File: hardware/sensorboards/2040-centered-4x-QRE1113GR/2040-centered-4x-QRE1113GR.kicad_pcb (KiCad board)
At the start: 2 copper layers, 49 x 46.5 mm, 15 parts, among them J1 Conn_01x10_Male, U1 QRE1113GR, U2 QRE1113GR, U3 QRE1113GR, U4 QRE1113GR

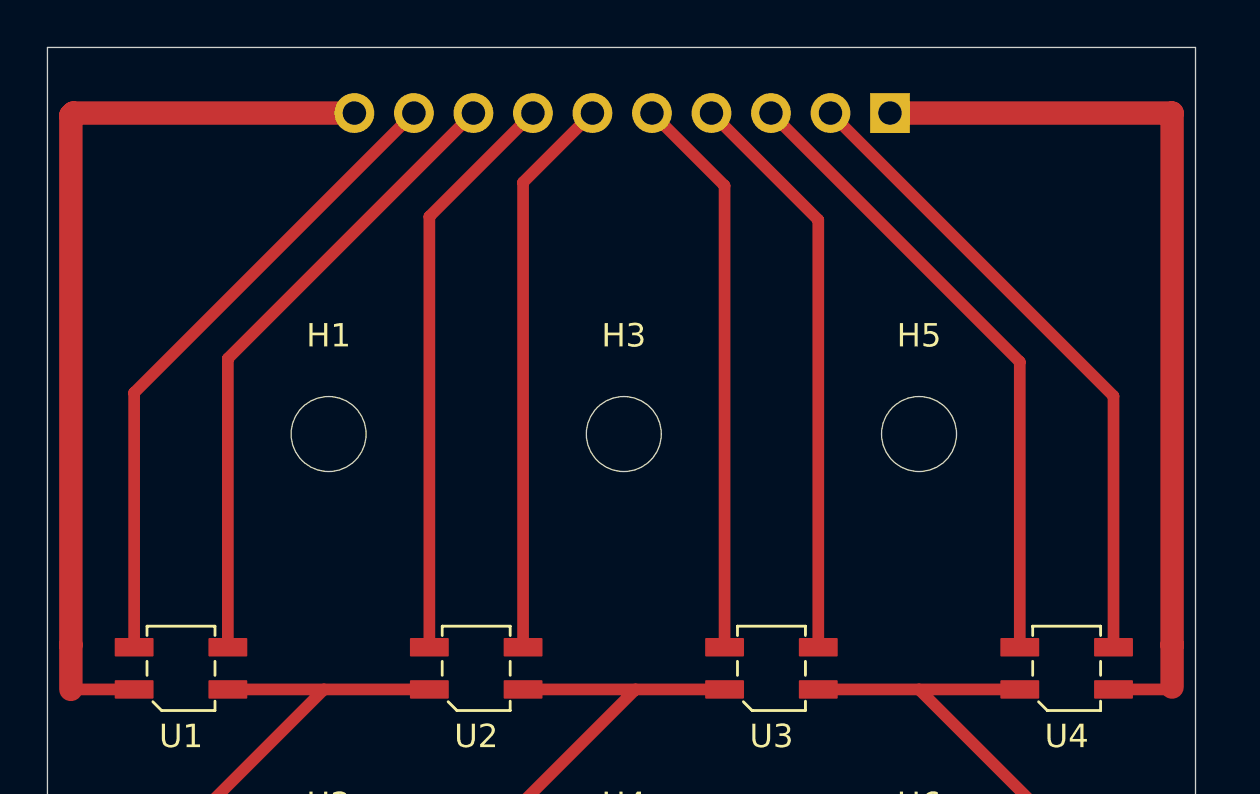
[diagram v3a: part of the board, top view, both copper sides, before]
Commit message: further suggestions from https://pianoclack.com/forum/d/542-update-on-piano-conversion/14
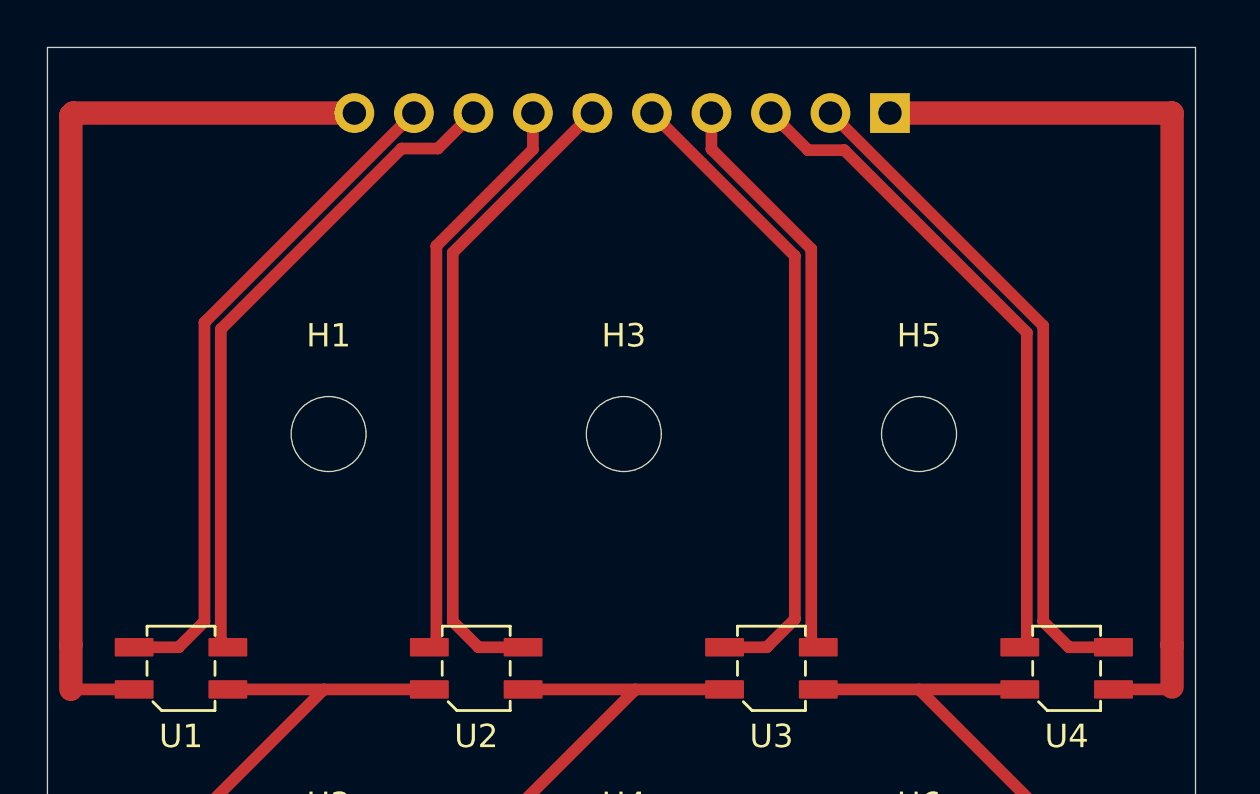
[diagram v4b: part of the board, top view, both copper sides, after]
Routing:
- net Net-(U2-Pad3): track 24.0 -> 27.6 mm
- net /E3: track 24.3 -> 27.6 mm
- net /E4: track 27.2 -> 28.4 mm
- net /C1: track 27.1 -> 28.3 mm
- net /E1: track 27.7 -> 28.9 mm
- net /C4: track 28.2 -> 28.9 mm
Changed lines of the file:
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@@
   (segment (start 159.5 92.9) (end 161.9 92.9) (width 0.5) (layer "F.Cu") (net 1))
   (segment (start 161.9 92.9) (end 162 92.8) (width 0.5) (layer "F.Cu") (net 1))
-  (segment (start 155.5 78.92) (end 155.5 91.1) (width 0.5) (layer "F.Cu") (net 2))
-  (segment (start 144.88 68.3) (end 155.5 78.92) (width 0.5) (layer "F.Cu") (net 2))
-  (segment (start 159.5 80.38) (end 147.42 68.3) (width 0.5) (layer "F.Cu") (net 3))
-  (segment (start 159.5 91.1) (end 159.5 80.38) (width 0.5) (layer "F.Cu") (net 3))
-  (segment (start 159.5 91.1) (end 159.1 91.1) (width 0.5) (layer "F.Cu") (net 3))
-  (segment (start 142.9 71.4) (end 142.9 91.1) (width 0.5) (layer "F.Cu") (net 4))
-  (segment (start 139.8 68.3) (end 142.9 71.4) (width 0.5) (layer "F.Cu") (net 4))
-  (segment (start 140 68.535) (end 139.84 68.375) (width 0.5) (layer "F.Cu") (net 4))
-  (segment (start 146.9 72.86) (end 146.9 91.1) (width 0.5) (layer "F.Cu") (net 5))
-  (segment (start 142.34 68.3) (end 146.9 72.86) (width 0.5) (layer "F.Cu") (net 5))
-  (segment (start 130.3 72.72) (end 130.3 91.1) (width 0.5) (layer "F.Cu") (net 6))
-  (segment (start 134.72 68.3) (end 130.3 72.72) (width 0.5) (layer "F.Cu") (net 6))
-  (segment (start 117.7 80.24) (end 129.64 68.3) (width 0.5) (layer "F.Cu") (net 7))
-  (segment (start 117.7 91.1) (end 117.7 80.24) (width 0.5) (layer "F.Cu") (net 7))
-  (segment (start 121.7 78.78) (end 121.7 91.1) (width 0.5) (layer "F.Cu") (net 8))
-  (segment (start 132.18 68.3) (end 121.7 78.78) (width 0.5) (layer "F.Cu") (net 8))
+  (segment (start 155.8 90.8) (end 155.8 77.66927) (width 0.5) (layer "F.Cu") (net 2))
+  (segment (start 146.464635 69.884635) (end 144.88 68.3) (width 0.5) (layer "F.Cu") (net 2))
+  (segment (start 155.8 77.66927) (end 148.015365 69.884635) (width 0.5) (layer "F.Cu") (net 2))
+  (segment (start 148.015365 69.884635) (end 146.464635 69.884635) (width 0.5) (layer "F.Cu") (net 2))
+  (segment (start 155.5 91.1) (end 155.8 90.8) (width 0.5) (layer "F.Cu") (net 2))
+  (segment (start 157.59952 91.1) (end 159.5 91.1) (width 0.5) (layer "F.Cu") (net 3))
+  (segment (start 147.42 68.3) (end 156.49952 77.37952) (width 0.5) (layer "F.Cu") (net 3))
+  (segment (start 156.49952 77.37952) (end 156.49952 90) (width 0.5) (layer "F.Cu") (net 3))
+  (segment (start 156.49952 90) (end 157.59952 91.1) (width 0.5) (layer "F.Cu") (net 3))
+  (segment (start 145.90048 89.89952) (end 144.7 91.1) (width 0.5) (layer "F.Cu") (net 4))
+  (segment (start 145.90048 74.40048) (end 139.8 68.3) (width 0.5) (layer "F.Cu") (net 4))
+  (segment (start 144.7 91.1) (end 142.9 91.1) (width 0.5) (layer "F.Cu") (net 4))
+  (segment (start 145.90048 74.40048) (end 145.90048 89.89952) (width 0.5) (layer "F.Cu") (net 4))
+  (segment (start 142.34 69.84) (end 146.6 74.1) (width 0.5) (layer "F.Cu") (net 5))
+  (segment (start 142.34 68.3) (end 142.34 69.84) (width 0.5) (layer "F.Cu") (net 5))
+  (segment (start 146.6 90.8) (end 146.9 91.1) (width 0.5) (layer "F.Cu") (net 5))
+  (segment (start 146.6 74.1) (end 146.6 90.8) (width 0.5) (layer "F.Cu") (net 5))
+  (segment (start 130.6 90.8) (end 130.6 73.97073) (width 0.5) (layer "F.Cu") (net 6))
+  (segment (start 134.72 69.85073) (end 134.72 68.3) (width 0.5) (layer "F.Cu") (net 6))
+  (segment (start 130.6 73.97073) (end 134.72 69.85073) (width 0.5) (layer "F.Cu") (net 6))
+  (segment (start 130.3 91.1) (end 130.6 90.8) (width 0.5) (layer "F.Cu") (net 6))
+  (segment (start 129.64 68.3) (end 120.700481 77.239519) (width 0.5) (layer "F.Cu") (net 7))
+  (segment (start 120.700481 89.999519) (end 119.6 91.1) (width 0.5) (layer "F.Cu") (net 7))
+  (segment (start 120.700481 77.239519) (end 120.700481 89.999519) (width 0.5) (layer "F.Cu") (net 7))
+  (segment (start 119.6 91.1) (end 117.7 91.1) (width 0.5) (layer "F.Cu") (net 7))
+  (segment (start 129.114635 69.814635) (end 121.4 77.52927) (width 0.5) (layer "F.Cu") (net 8))
+  (segment (start 121.4 90.8) (end 121.7 91.1) (width 0.5) (layer "F.Cu") (net 8))
+  (segment (start 121.4 77.52927) (end 121.4 90.8) (width 0.5) (layer "F.Cu") (net 8))
+  (segment (start 130.665365 69.814635) (end 129.114635 69.814635) (width 0.5) (layer "F.Cu") (net 8))
+  (segment (start 132.18 68.3) (end 130.665365 69.814635) (width 0.5) (layer "F.Cu") (net 8))
   (segment (start 115 92.9) (end 117.7 92.9) (width 0.5) (layer "F.Cu") (net 9))
   (segment (start 115.1 68.3) (end 127.1 68.3) (width 1) (layer "F.Cu") (net 9))
@@
   (segment (start 146.9 92.9) (end 155.5 92.9) (width 0.5) (layer "F.Cu") (net 12))
   (segment (start 158 99.7) (end 151.2 92.9) (width 0.5) (layer "F.Cu") (net 12))
-  (segment (start 137.26 68.3) (end 134.3 71.26) (width 0.5) (layer "F.Cu") (net 13))
-  (segment (start 134.3 71.26) (end 134.3 91.1) (width 0.5) (layer "F.Cu") (net 13))
+  (segment (start 131.29952 74.26048) (end 131.29952 90) (width 0.5) (layer "F.Cu") (net 13))
+  (segment (start 132.39952 91.1) (end 134.3 91.1) (width 0.5) (layer "F.Cu") (net 13))
+  (segment (start 137.26 68.3) (end 131.29952 74.26048) (width 0.5) (layer "F.Cu") (net 13))
+  (segment (start 131.29952 90) (end 132.39952 91.1) (width 0.5) (layer "F.Cu") (net 13))
 )
